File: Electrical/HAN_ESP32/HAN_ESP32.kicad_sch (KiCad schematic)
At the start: 30 parts, among them J1 8P8C_Shielded, J2 USB_B_Micro, J3 Conn_01x06, Q1 BSS84, SW1 ESP_RESET, SW2 ESP_PROG, U1 AP7375-33SA, U2 ESP32-WROOM-32, U3 TSS721

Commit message: Initial layout done
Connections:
- net GND: now also J1.SH
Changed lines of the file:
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@@
+    (stroke (width 0) (type default) (color 0 0 0 0))
+  )
+  (wire (pts (xy 44.45 86.36) (xy 49.53 86.36))
     (stroke (width 0) (type default) (color 0 0 0 0))
   )
@@
   )
   (wire (pts (xy 54.61 99.06) (xy 60.96 99.06))
+    (stroke (width 0) (type default) (color 0 0 0 0))
+  )
+  (wire (pts (xy 44.45 91.44) (xy 44.45 86.36))
     (stroke (width 0) (type default) (color 0 0 0 0))
   )
@@
     )
     (property "Datasheet" "~" (id 3) (at 46.99 34.29 0)
+      (effects (font (size 1.27 1.27)) hide)
+    )
+    (pin "1")
+  )
+  (symbol (lib_id "power:GND") (at 49.53 86.36 0) (unit 1)
+    (in_bom yes) (on_board yes) (fields_autoplaced)
+    (property "Reference" "#PWR?" (id 0) (at 49.53 92.71 0)
+      (effects (font (size 1.27 1.27)) hide)
+    )
+    (property "Value" "GND" (id 1) (at 49.53 91.44 0))
+    (property "Footprint" "" (id 2) (at 49.53 86.36 0)
+      (effects (font (size 1.27 1.27)) hide)
+    )
+    (property "Datasheet" "" (id 3) (at 49.53 86.36 0)
       (effects (font (size 1.27 1.27)) hide)
     )
@@
       (reference "#PWR0110") (unit 1) (value "GND") (footprint "")
     )
+    (path "/9794808f-537c-446b-9d03-a56ce60b80e5"
+      (reference "#PWR?") (unit 1) (value "GND") (footprint "")
+    )
     (path "/1b949d4f-12b2-4be4-9280-c320374d3a44"

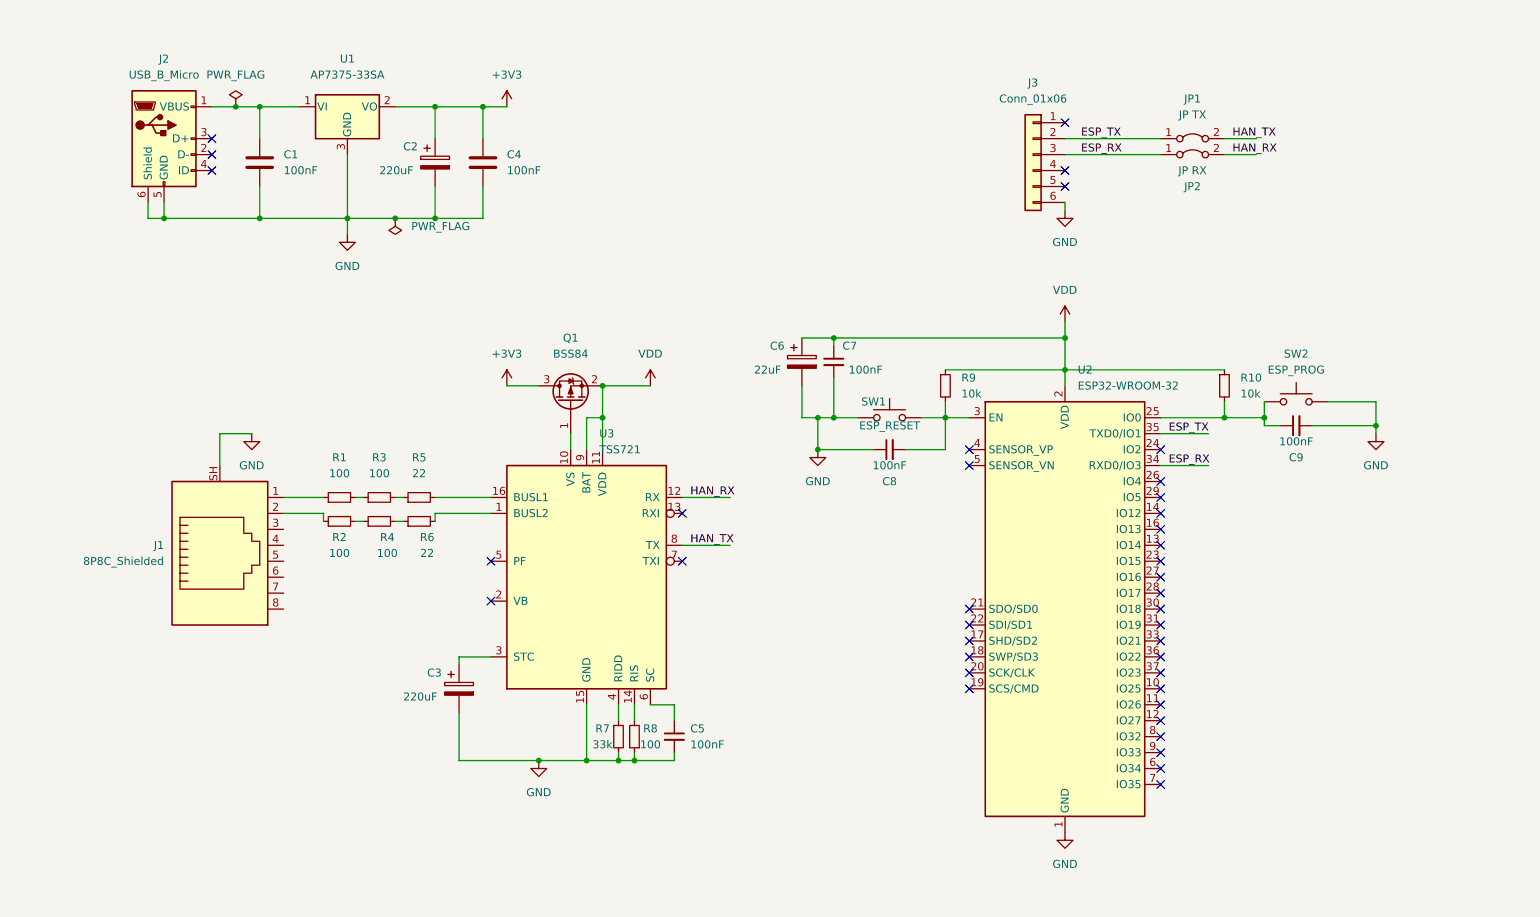
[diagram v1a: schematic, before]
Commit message: Add some information and comments in schematic; add BSS84 datasheet; fix micro USB 3D model
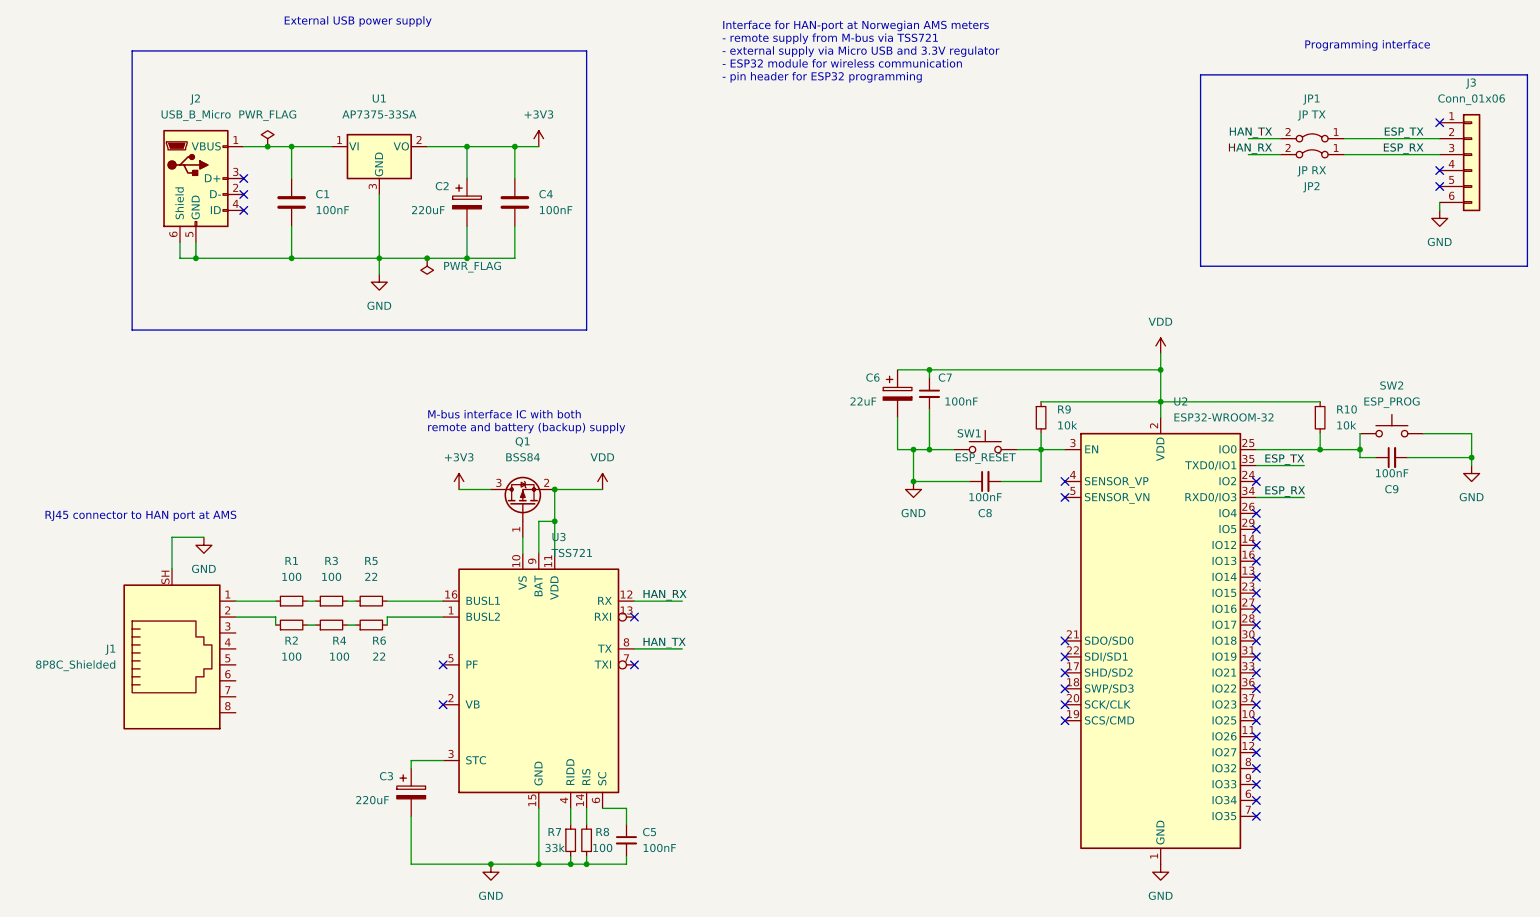
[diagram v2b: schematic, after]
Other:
- note added: "External USB power supply"
- note added: "Interface for HAN-port at Norwegian AMS meters - remote supply from M-bus via TSS721 - external supply via Micro USB and 3.3V regulator - ESP32 module for wireless communication - pin header for ESP32 programming"
- note added: "M-bus interface IC with both remote and battery (backup) supply"
- note added: "Programming interface"
- note added: "RJ45 connector to HAN port at AMS"
- company: (none) -> Robert Braunschweig
- title: (none) -> HAN-port sensor
- moved on the sheet: C1, C2, C3, C4, C5, C6, C7, C8, C9, J1, J2, J3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
